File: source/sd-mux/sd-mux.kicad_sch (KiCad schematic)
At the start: 60 parts, among them IC1 NCP1117DT33G, IC2 FT260S-U, J1 USB_B_Micro, J2 Micro_SD_Card_Det, U1 USB2641I-HZH-02, U4 TS3A27518EPW, U5 SD_CONNECTOR, Y1 24MHz

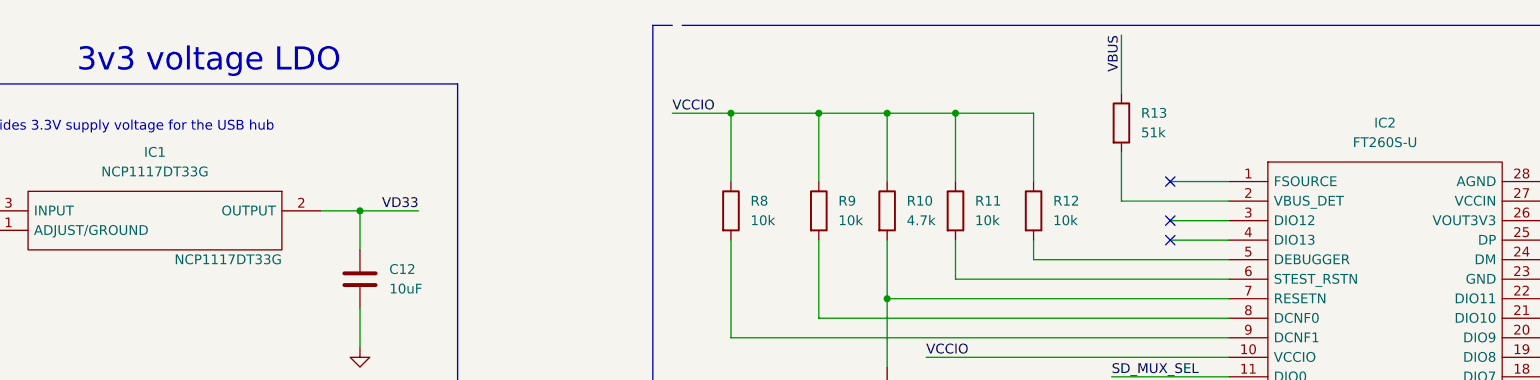
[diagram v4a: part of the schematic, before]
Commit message: make first set of fixes for prototyping
Change-type: patch
Signed-off-by: Ryan Cooke <ryan@balena.io>
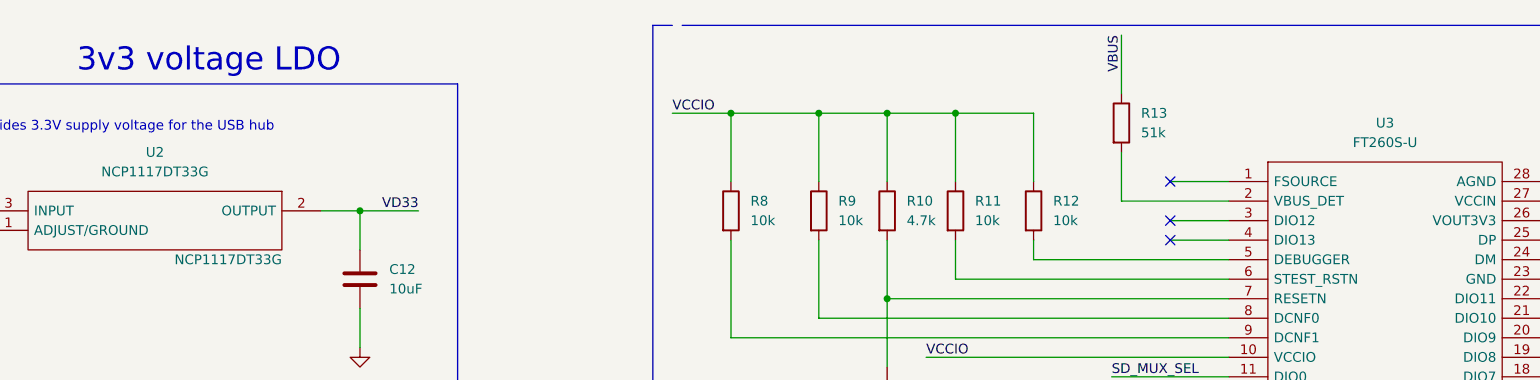
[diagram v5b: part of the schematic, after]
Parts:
- Y1: footprint Crystal:Crystal_SMD_2016-4Pin_2.0x1.6mm -> Crystal:Crystal_SMD_2012-2Pin_2.0x1.2mm
- renumbered IC1 to U2, IC2 to U3
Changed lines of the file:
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@@
   (symbol (lib_id "FT260S-U:FT260S-U") (at 308.61 35.56 0) (unit 1)
     (in_bom yes) (on_board yes) (fields_autoplaced)
-    (property "Reference" "IC2" (id 0) (at 328.93 27.94 0))
+    (property "Reference" "U3" (id 0) (at 328.93 27.94 0))
     (property "Value" "FT260S-U" (id 1) (at 328.93 30.48 0))
     (property "Footprint" "SOP65P640X120-28N" (id 2) (at 345.44 33.02 0)
@@
     (property "Reference" "Y1" (id 0) (at 72.39 236.22 0))
     (property "Value" "24MHz" (id 1) (at 72.39 238.76 0))
-    (property "Footprint" "Crystal:Crystal_SMD_2016-4Pin_2.0x1.6mm" (id 2) (at 72.39 243.84 0)
+    (property "Footprint" "Crystal:Crystal_SMD_2012-2Pin_2.0x1.2mm" (id 2) (at 72.39 243.84 0)
       (effects (font (size 1.27 1.27)) hide)
     )
@@
       (effects (font (size 1.27 1.27)) hide)
     )
+    (pin "1")
+    (pin "2")
+    (pin "3")
+    (pin "4")
     (pin "5")
-    (pin "3")
+    (pin "6")
     (pin "7")
     (pin "8")
-    (pin "1")
-    (pin "2")
-    (pin "4")
-    (pin "6")
   )
   (symbol (lib_id "Device:FerriteBead") (at 59.69 62.23 0) (unit 1)
@@
   (symbol (lib_id "NCP1117DT33G:NCP1117DT33G") (at 158.75 40.64 0) (unit 1)
     (in_bom yes) (on_board yes)
-    (property "Reference" "IC1" (id 0) (at 168.91 31.75 0))
+    (property "Reference" "U2" (id 0) (at 168.91 31.75 0))
     (property "Value" "NCP1117DT33G" (id 1) (at 168.91 34.29 0))
     (property "Footprint" "NCP1117DT33G" (id 2) (at 171.45 45.72 0)
@@
       (reference "FB4") (unit 1) (value "2A/0.05DCR") (footprint "Resistor_SMD:R_0201_0603Metric")
     )
-    (path "/a81a2dad-f917-417a-a540-2d334f0ac69e"
-      (reference "IC1") (unit 1) (value "NCP1117DT33G") (footprint "NCP1117DT33G")
-    )
-    (path "/72d6dbc1-4f75-4624-8c15-96b317920b01"
-      (reference "IC2") (unit 1) (value "FT260S-U") (footprint "SOP65P640X120-28N")
-    )
     (path "/e45c3082-4d8d-4bd3-a08e-18a1f9826960"
       (reference "J1") (unit 1) (value "USB_B_Micro") (footprint "Connector_USB:USB_Micro-B_Wuerth_629105150521_CircularHoles")
@@
       (reference "U1") (unit 1) (value "USB2641I-HZH-02") (footprint "QFN50P700X700X100-49N-D")
     )
+    (path "/a81a2dad-f917-417a-a540-2d334f0ac69e"
+      (reference "U2") (unit 1) (value "NCP1117DT33G") (footprint "NCP1117DT33G")
+    )
+    (path "/72d6dbc1-4f75-4624-8c15-96b317920b01"
+      (reference "U3") (unit 1) (value "FT260S-U") (footprint "SOP65P640X120-28N")
+    )
     (path "/a41e579d-ae08-4be3-8e7f-c581fb40aafc"
       (reference "U4") (unit 1) (value "TS3A27518EPW") (footprint "Package_SO:TSSOP-24_4.4x7.8mm_P0.65mm")
@@
     )
     (path "/a16cfd73-6e44-4daf-ab2b-01b13a9b1e74"
-      (reference "Y1") (unit 1) (value "24MHz") (footprint "Crystal:Crystal_SMD_2016-4Pin_2.0x1.6mm")
-    )
-  )
+      (reference "Y1") (unit 1) (value "24MHz") (footprint "Crystal:Crystal_SMD_2012-2Pin_2.0x1.2mm")
+    )
+  )

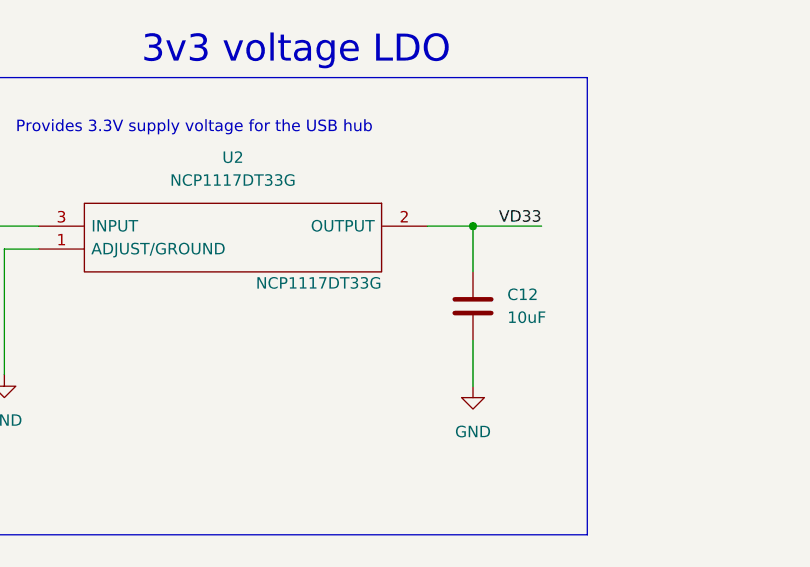
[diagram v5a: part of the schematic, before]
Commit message: change footprints to 0603 and add parts to bom
Change-type: patch
Signed-off-by: Ryan Cooke <ryan@balena.io>
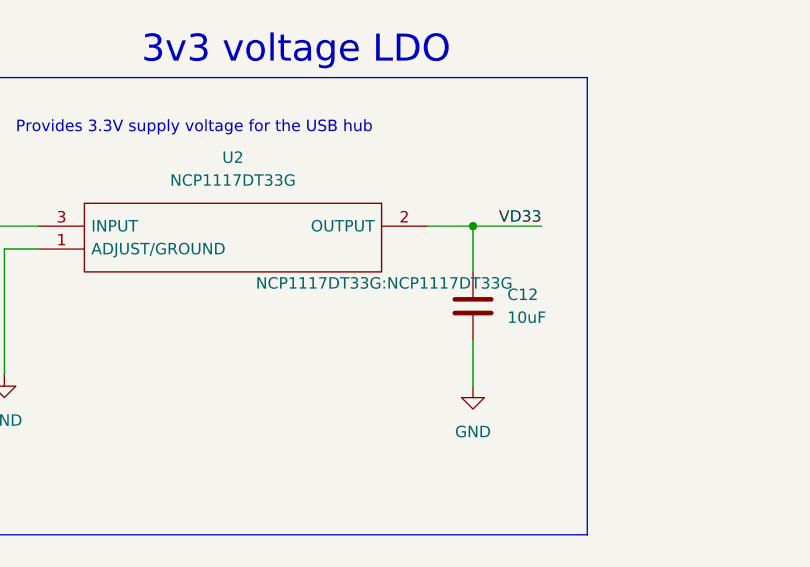
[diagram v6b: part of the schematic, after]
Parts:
- C1, C10, C11, C12, C13, C14, C15, C16, C17, C18, C19, C2, C20, C21, C22, C23, C24, C25, C26, C3, C4, C5, C6, C7, C8, C9: footprint Capacitor_SMD:C_0201_0603Metric -> Capacitor_SMD:C_0603_1608Metric
- D1, D2, D3: footprint LED_SMD:LED_0201_0603Metric -> LED_SMD:LED_0603_1608Metric
- FB1, FB2, FB3, FB4, R1, R10, R11, R12, R13, R14, R15, R16, R17, R18, R19, R2, R3, R4, R5, R6, R7, R8, R9: footprint Resistor_SMD:R_0201_0603Metric -> Resistor_SMD:R_0603_1608Metric
- U1: footprint QFN50P700X700X100-49N-D -> USB2461I-HZH-02:QFN50P700X700X100-49N-D
- U2: footprint NCP1117DT33G -> NCP1117DT33G:NCP1117DT33G
- U3: footprint SOP65P640X120-28N -> FT260:SOP65P640X120-28N
- Y1: footprint Crystal:Crystal_SMD_2012-2Pin_2.0x1.2mm -> Crystal:Crystal_SMD_2016-4Pin_2.0x1.6mm
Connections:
- net XTAL2: now also Y1.3; no longer Y1.2
